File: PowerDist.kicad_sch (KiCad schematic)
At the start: 18 parts, among them J7 PowerConn, Q1 Q_PMOS_GSD, U2 RI3-1205S, U3 LD1117-3.3_SOT223

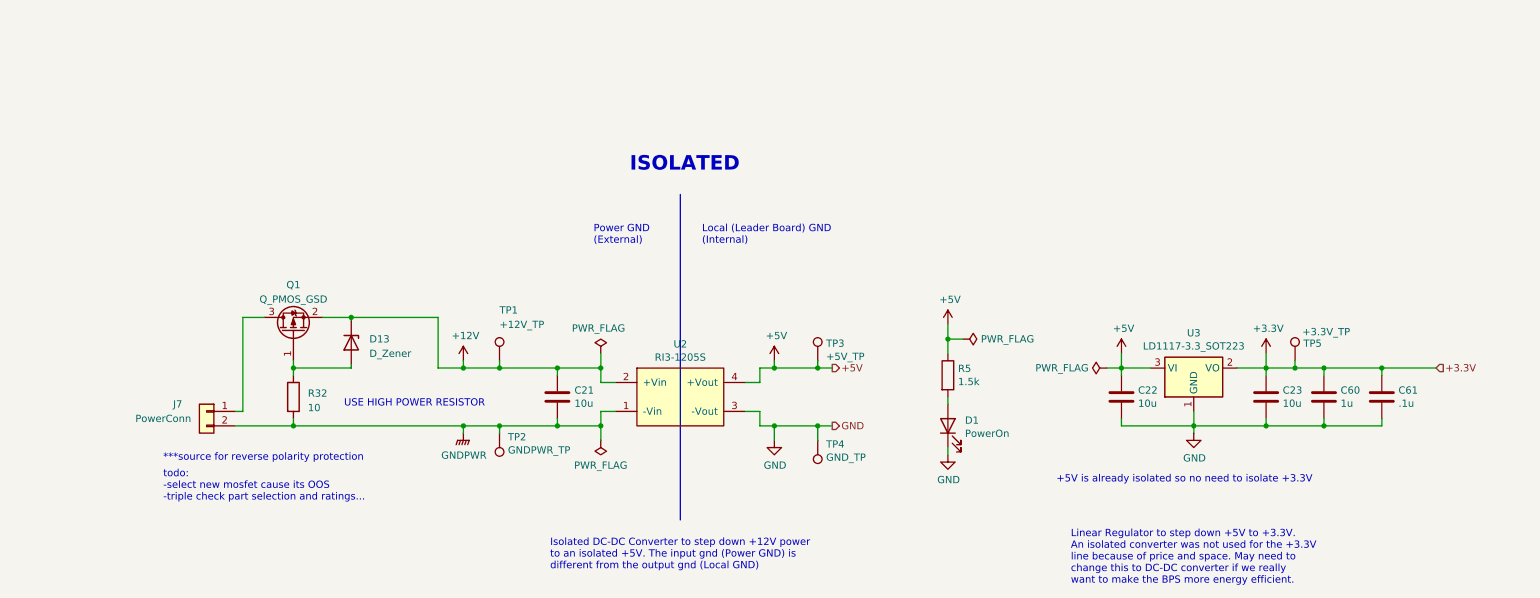
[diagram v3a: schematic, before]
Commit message: inputs routing + fixed models + clock keepouts
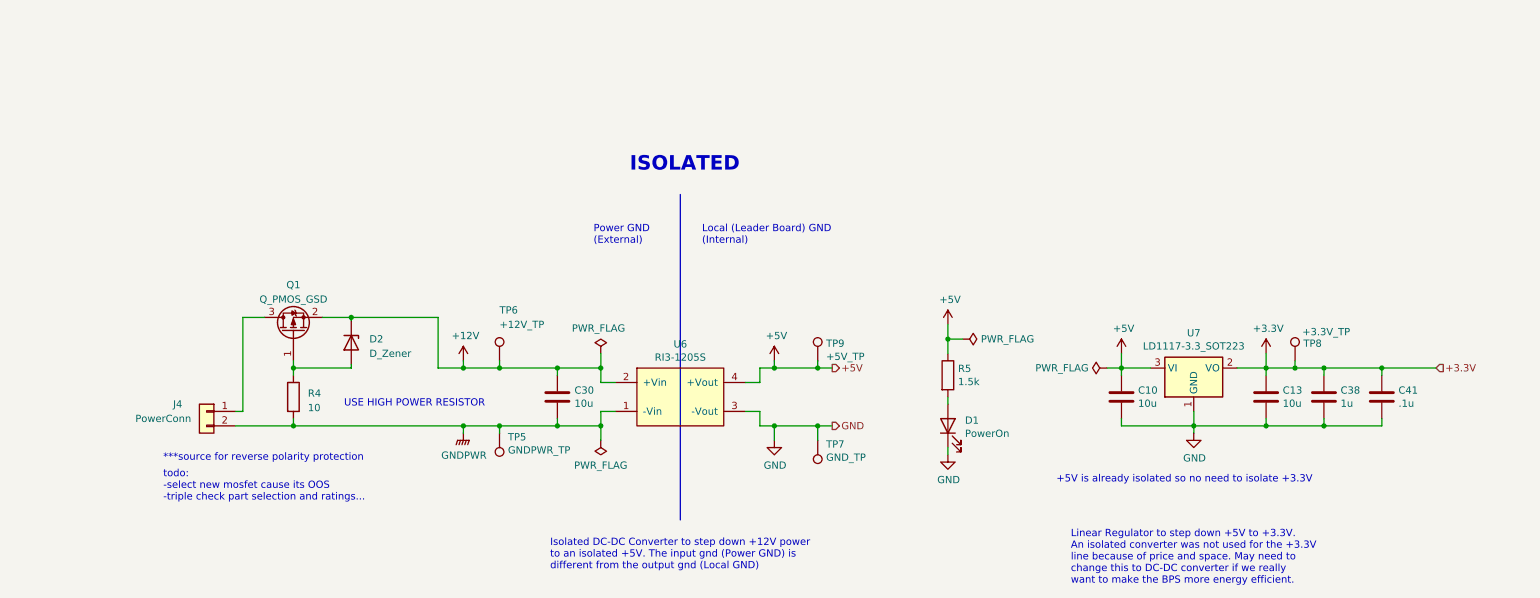
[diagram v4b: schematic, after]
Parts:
- renumbered C22 to C10, C23 to C13, C21 to C30, C60 to C38, C61 to C41, D13 to D2, J7 to J4, R32 to R4, TP2 to TP5, TP1 to TP6, TP4 to TP7, TP5 to TP8, TP3 to TP9, U2 to U6, U3 to U7
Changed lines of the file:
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@@
   (symbol (lib_id "Device:C") (at 113.03 89.535 0) (unit 1)
     (in_bom yes) (on_board yes) (dnp no)
-    (property "Reference" "C21" (at 116.0272 88.3666 0)
+    (property "Reference" "C30" (at 116.0272 88.3666 0)
       (effects (font (size 1.27 1.27)) (justify left))
     )
@@
       (project "Telemetry-Primary"
         (path "/7f2a449b-14af-42b3-8d38-5f0f8a5ee7ce/00000000-0000-0000-0000-00005f6cdfd6"
-          (reference "C21") (unit 1)
+          (reference "C30") (unit 1)
         )
       )
@@
   (symbol (lib_id "Connector:TestPoint") (at 102.87 83.185 0) (unit 1)
     (in_bom yes) (on_board yes) (dnp no)
-    (property "Reference" "TP1" (at 102.87 74.295 0)
+    (property "Reference" "TP6" (at 102.87 74.295 0)
       (effects (font (size 1.27 1.27)) (justify left))
     )
@@
       (project "Telemetry-Primary"
         (path "/7f2a449b-14af-42b3-8d38-5f0f8a5ee7ce/00000000-0000-0000-0000-00005f6cdfd6"
-          (reference "TP1") (unit 1)
+          (reference "TP6") (unit 1)
         )
       )
@@
   (symbol (lib_id "Connector:TestPoint") (at 158.75 83.185 0) (unit 1)
     (in_bom yes) (on_board yes) (dnp no)
-    (property "Reference" "TP3" (at 160.2232 80.137 0)
+    (property "Reference" "TP9" (at 160.2232 80.137 0)
       (effects (font (size 1.27 1.27)) (justify left))
     )
@@
       (project "Telemetry-Primary"
         (path "/7f2a449b-14af-42b3-8d38-5f0f8a5ee7ce/00000000-0000-0000-0000-00005f6cdfd6"
-          (reference "TP3") (unit 1)
+          (reference "TP9") (unit 1)
         )
       )
@@
   (symbol (lib_id "Connector:TestPoint") (at 158.75 97.155 180) (unit 1)
     (in_bom yes) (on_board yes) (dnp no)
-    (property "Reference" "TP4" (at 160.2232 97.8408 0)
+    (property "Reference" "TP7" (at 160.2232 97.8408 0)
       (effects (font (size 1.27 1.27)) (justify right))
     )
@@
       (project "Telemetry-Primary"
         (path "/7f2a449b-14af-42b3-8d38-5f0f8a5ee7ce/00000000-0000-0000-0000-00005f6cdfd6"
-          (reference "TP4") (unit 1)
+          (reference "TP7") (unit 1)
         )
       )
@@
   (symbol (lib_id "utsvt-power-regulators:RI3-1205S") (at 134.62 84.455 0) (unit 1)
     (in_bom yes) (on_board yes) (dnp no)
-    (property "Reference" "U2" (at 134.62 80.264 0)
+    (property "Reference" "U6" (at 134.62 80.264 0)
       (effects (font (size 1.27 1.27)))
     )
@@
       (project "Telemetry-Primary"
         (path "/7f2a449b-14af-42b3-8d38-5f0f8a5ee7ce/00000000-0000-0000-0000-00005f6cdfd6"
-          (reference "U2") (unit 1)
+          (reference "U6") (unit 1)
         )
       )
@@
   (symbol (lib_id "Regulator_Linear:LD1117S33TR_SOT223") (at 224.79 84.455 0) (unit 1)
     (in_bom yes) (on_board yes) (dnp no)
-    (property "Reference" "U3" (at 224.79 78.3082 0)
+    (property "Reference" "U7" (at 224.79 78.3082 0)
       (effects (font (size 1.27 1.27)))
     )
@@
       (project "Telemetry-Primary"
         (path "/7f2a449b-14af-42b3-8d38-5f0f8a5ee7ce/00000000-0000-0000-0000-00005f6cdfd6"
-          (reference "U3") (unit 1)
+          (reference "U7") (unit 1)
         )
       )
@@
   (symbol (lib_id "Device:C") (at 212.09 89.535 0) (unit 1)
     (in_bom yes) (on_board yes) (dnp no)
-    (property "Reference" "C22" (at 215.011 88.3666 0)
+    (property "Reference" "C10" (at 215.011 88.3666 0)
       (effects (font (size 1.27 1.27)) (justify left))
     )
@@
       (project "Telemetry-Primary"
         (path "/7f2a449b-14af-42b3-8d38-5f0f8a5ee7ce/00000000-0000-0000-0000-00005f6cdfd6"
-          (reference "C22") (unit 1)
+          (reference "C10") (unit 1)
         )
       )
@@
   (symbol (lib_id "Device:C") (at 237.49 89.535 0) (unit 1)
     (in_bom yes) (on_board yes) (dnp no)
-    (property "Reference" "C23" (at 240.411 88.3666 0)
+    (property "Reference" "C13" (at 240.411 88.3666 0)
       (effects (font (size 1.27 1.27)) (justify left))
     )
@@
       (project "Telemetry-Primary"
         (path "/7f2a449b-14af-42b3-8d38-5f0f8a5ee7ce/00000000-0000-0000-0000-00005f6cdfd6"
-          (reference "C23") (unit 1)
+          (reference "C13") (unit 1)
         )
       )
@@
   (symbol (lib_id "Connector:TestPoint") (at 242.57 83.185 0) (unit 1)
     (in_bom yes) (on_board yes) (dnp no)
-    (property "Reference" "TP5" (at 244.0432 80.137 0)
+    (property "Reference" "TP8" (at 244.0432 80.137 0)
       (effects (font (size 1.27 1.27)) (justify left))
     )
@@
       (project "Telemetry-Primary"
         (path "/7f2a449b-14af-42b3-8d38-5f0f8a5ee7ce/00000000-0000-0000-0000-00005f6cdfd6"
-          (reference "TP5") (unit 1)
+          (reference "TP8") (unit 1)
         )
       )
@@
   (symbol (lib_id "Connector:TestPoint") (at 102.87 95.885 180) (unit 1)
     (in_bom yes) (on_board yes) (dnp no)
-    (property "Reference" "TP2" (at 104.3432 96.5708 0)
+    (property "Reference" "TP5" (at 104.3432 96.5708 0)
       (effects (font (size 1.27 1.27)) (justify right))
     )
@@
       (project "Telemetry-Primary"
         (path "/7f2a449b-14af-42b3-8d38-5f0f8a5ee7ce/00000000-0000-0000-0000-00005f6cdfd6"
-          (reference "TP2") (unit 1)
+          (reference "TP5") (unit 1)
         )
       )
@@
   (symbol (lib_id "Connector_Generic:Conn_01x02") (at 51.435 92.075 0) (mirror y) (unit 1)
     (in_bom yes) (on_board yes) (dnp no)
-    (property "Reference" "J7" (at 46.355 90.805 0)
+    (property "Reference" "J4" (at 46.355 90.805 0)
       (effects (font (size 1.27 1.27)))
     )
@@
       (project "Telemetry-Primary"
         (path "/7f2a449b-14af-42b3-8d38-5f0f8a5ee7ce/00000000-0000-0000-0000-00005f6cdfd6"
-          (reference "J7") (unit 1)
+          (reference "J4") (unit 1)
         )
       )
@@
   (symbol (lib_id "Device:D_Zener") (at 76.835 80.01 270) (unit 1)
     (in_bom yes) (on_board yes) (dnp no) (fields_autoplaced)
-    (property "Reference" "D13" (at 80.01 79.375 90)
+    (property "Reference" "D2" (at 80.01 79.375 90)
       (effects (font (size 1.27 1.27)) (justify left))
     )
@@
       (project "Telemetry-Primary"
         (path "/7f2a449b-14af-42b3-8d38-5f0f8a5ee7ce/00000000-0000-0000-0000-00005f6cdfd6"
-          (reference "D13") (unit 1)
+          (reference "D2") (unit 1)
         )
       )
@@
   (symbol (lib_id "Device:R") (at 66.675 89.535 0) (unit 1)
     (in_bom yes) (on_board yes) (dnp no) (fields_autoplaced)
-    (property "Reference" "R32" (at 69.215 88.9 0)
+    (property "Reference" "R4" (at 69.215 88.9 0)
       (effects (font (size 1.27 1.27)) (justify left))
     )
@@
       (project "Telemetry-Primary"
         (path "/7f2a449b-14af-42b3-8d38-5f0f8a5ee7ce/00000000-0000-0000-0000-00005f6cdfd6"
-          (reference "R32") (unit 1)
+          (reference "R4") (unit 1)
         )
       )
@@
   (symbol (lib_id "Device:C") (at 247.65 89.535 0) (unit 1)
     (in_bom yes) (on_board yes) (dnp no)
-    (property "Reference" "C60" (at 250.571 88.3666 0)
+    (property "Reference" "C38" (at 250.571 88.3666 0)
       (effects (font (size 1.27 1.27)) (justify left))
     )
@@
       (project "Telemetry-Primary"
         (path "/7f2a449b-14af-42b3-8d38-5f0f8a5ee7ce/00000000-0000-0000-0000-00005f6cdfd6"
-          (reference "C60") (unit 1)
+          (reference "C38") (unit 1)
         )
       )
@@
   (symbol (lib_id "Device:C") (at 257.81 89.535 0) (unit 1)
     (in_bom yes) (on_board yes) (dnp no)
-    (property "Reference" "C61" (at 260.731 88.3666 0)
+    (property "Reference" "C41" (at 260.731 88.3666 0)
       (effects (font (size 1.27 1.27)) (justify left))
     )
@@
       (project "Telemetry-Primary"
         (path "/7f2a449b-14af-42b3-8d38-5f0f8a5ee7ce/00000000-0000-0000-0000-00005f6cdfd6"
-          (reference "C61") (unit 1)
-        )
-      )
+          (reference "C41") (unit 1)
+        )
+      )
